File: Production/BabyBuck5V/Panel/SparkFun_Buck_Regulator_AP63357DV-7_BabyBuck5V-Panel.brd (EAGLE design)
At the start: 150.6 x 96 mm, 1446 parts, among them U1 AP63357, U10 AP63357, U11 AP63357, U12 AP63357, U13 AP63357, U14 AP63357, U15 AP63357, U16 AP63357, U17 AP63357, U18 AP63357, U19 AP63357, U2 AP63357, U20 AP63357, U21 AP63357, U22 AP63357, U23 AP63357, U24 AP63357, U25 AP63357, U26 AP63357, U27 AP63357, U28 AP63357, U29 AP63357, U3 AP63357, U30 AP63357, U31 AP63357, U32 AP63357, U33 AP63357, U34 AP63357, U35 AP63357, U36 AP63357, U37 AP63357, U38 AP63357, U39 AP63357, U4 AP63357, U40 AP63357, U41 AP63357, U42 AP63357, U43 AP63357, U44 AP63357, U45 AP63357, U46 AP63357, U47 AP63357, U48 AP63357, U5 AP63357, U6 AP63357, U7 AP63357, U8 AP63357, U9 AP63357

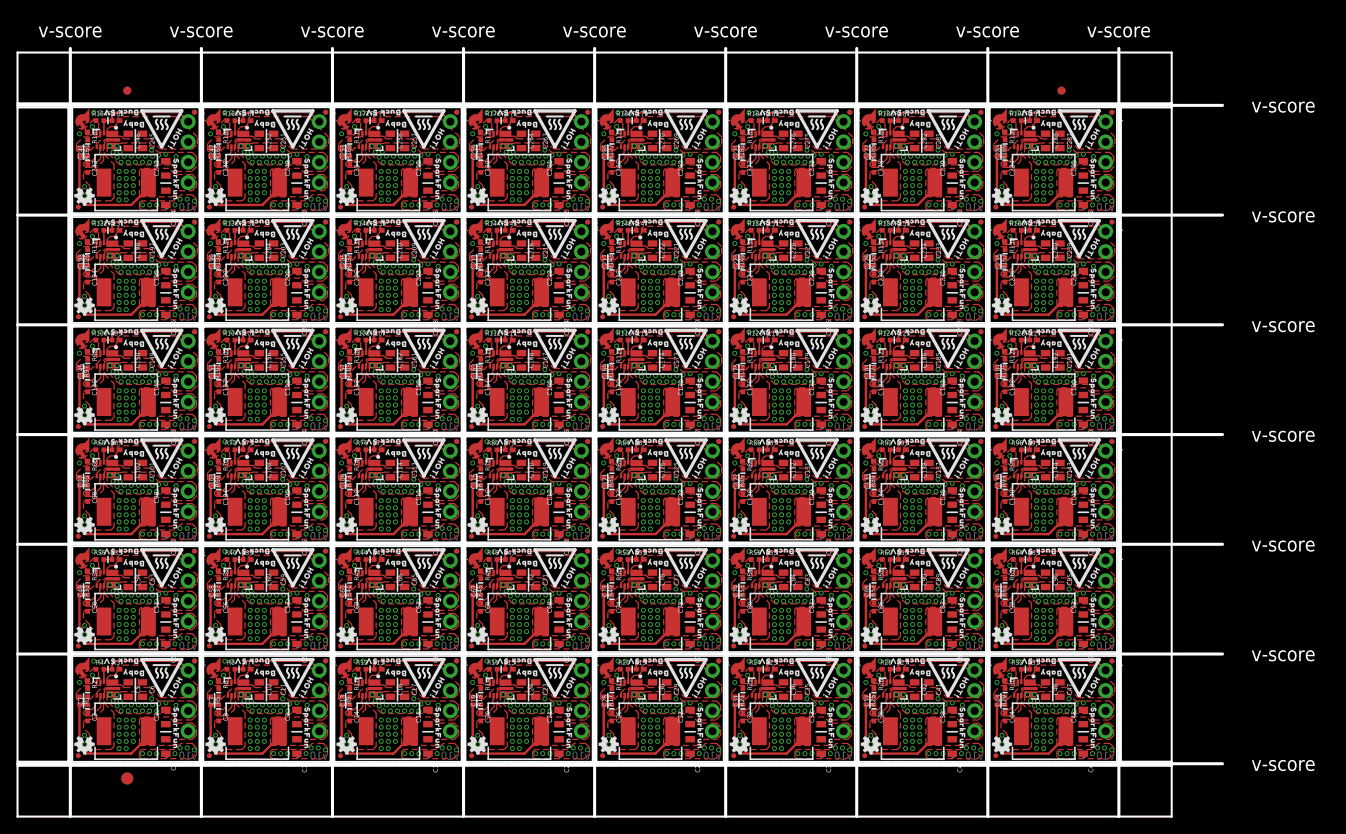
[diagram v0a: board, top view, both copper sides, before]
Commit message: Prepare for v10 reds order.
Change R1/R2 to better match 5V output requirement.
Repanelize.
Reorganize Production Folder Structure.
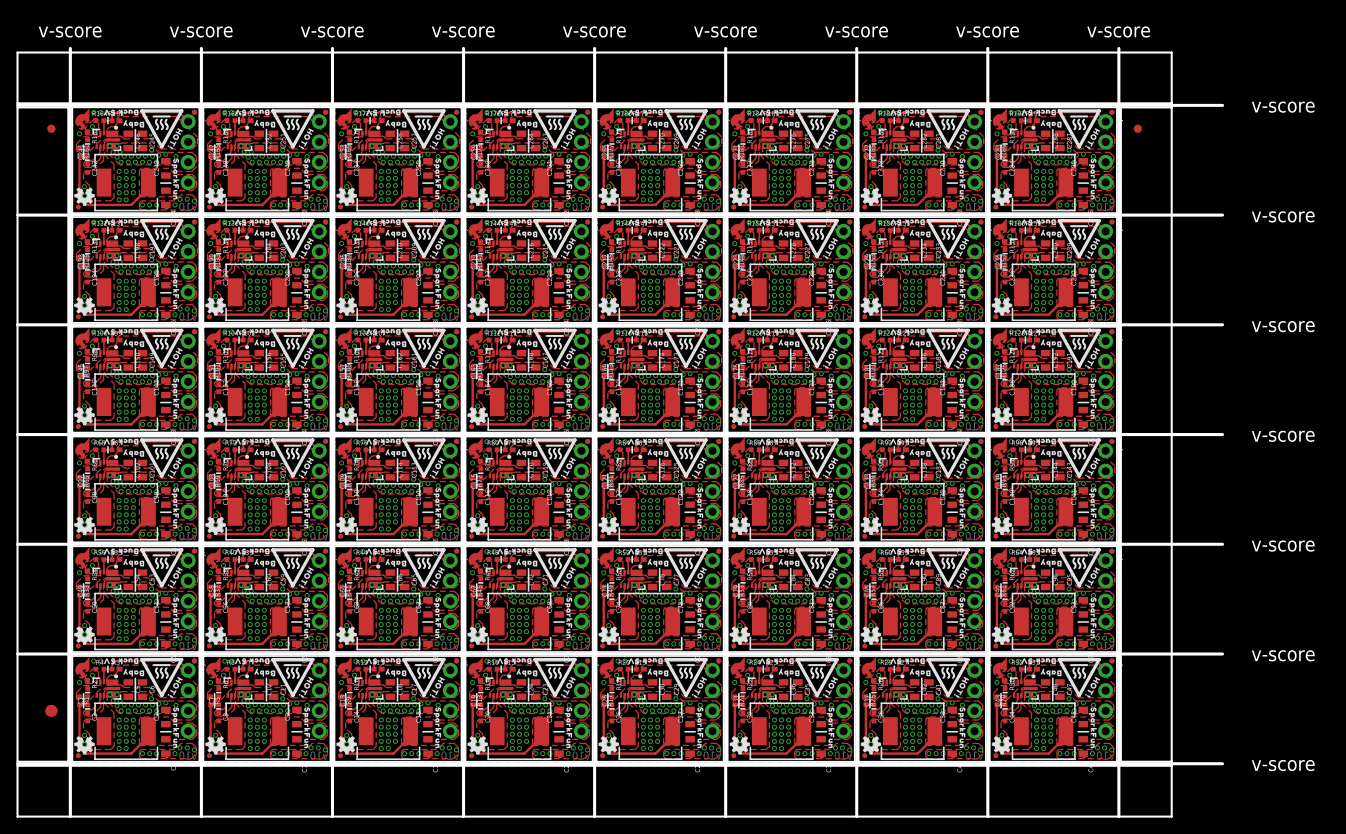
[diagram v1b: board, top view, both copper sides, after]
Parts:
- R1, R101, R105, R109, R113, R117, R121, R125, R129, R13, R133, R137, R141, R145, R149, R153, R157, R161, R165, R169, R17, R173, R177, R181, R185, R189, R21, R25, R29, R33, R37, R41, R45, R49, R5, R53, R57, R61, R65, R69, R73, R77, R81, R85, R89, R9, R93, R97: value 150k -> 220K
- R10, R102, R106, R110, R114, R118, R122, R126, R130, R134, R138, R14, R142, R146, R150, R154, R158, R162, R166, R170, R174, R178, R18, R182, R186, R190, R2, R22, R26, R30, R34, R38, R42, R46, R50, R54, R58, R6, R62, R66, R70, R74, R78, R82, R86, R90, R94, R98: value 28.7k -> 41.2K
- moved E$5 12.7 mm to (-2.62, 6.35)
- moved E$6 12.7 mm to (-2.62, 6.35)
- moved E$3 10.7 mm to (133.2, 79.1)
- moved E$4 10.7 mm to (133.2, 79.1)
- moved E$1 10.6 mm to (-2.62, 79.1)
- moved E$2 10.6 mm to (-2.62, 79.1)
